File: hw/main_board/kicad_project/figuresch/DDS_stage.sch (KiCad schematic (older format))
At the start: 12 parts

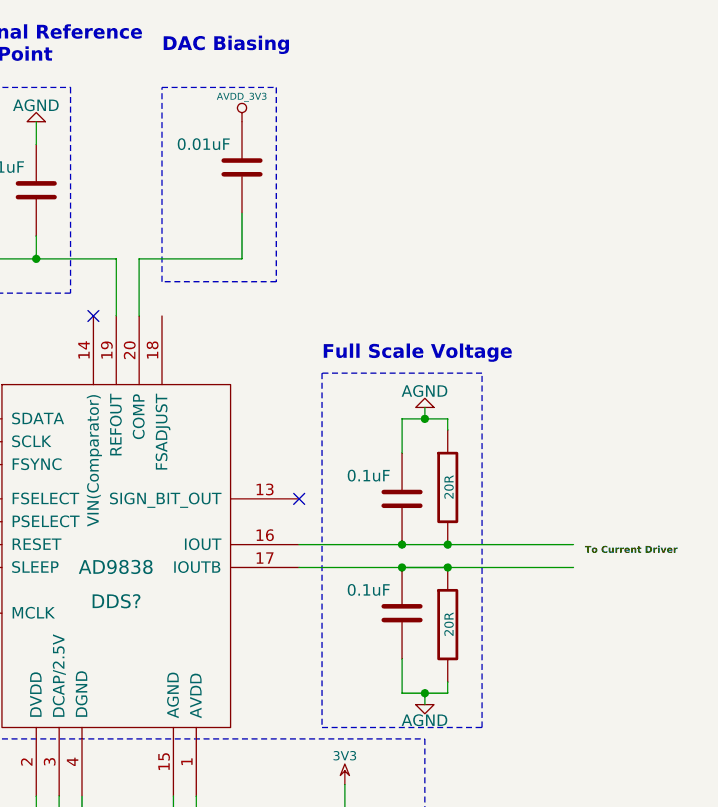
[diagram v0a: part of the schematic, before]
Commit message: started mainboard pcb layout, fixing small things in schematic, TODO: schematic connector symbols and pads
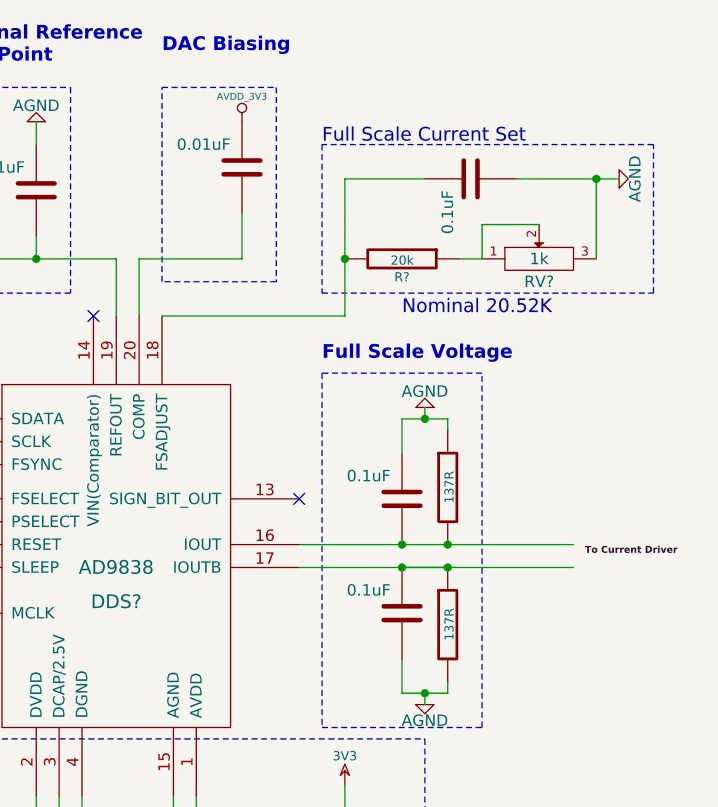
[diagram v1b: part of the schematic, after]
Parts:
- added C?: 0.1uF, symbol C
- added R?: 20k, symbol R
- added RV?: 1k, symbol POT
- R? (x2): value 20R -> 137R
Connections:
- wire segments 38 -> 46
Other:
- note added: "Full Scale Current Set"
- note added: "Nominal 20.52K\n"
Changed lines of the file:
@@
 LIBS:contrib
 LIBS:valves
-LIBS:tDCS_driver-cache
+LIBS:DDS_stage-cache
 EELAYER 24 0
 EELAYER END
@@
 P 6800 3250
 F 0 "R?" H 6880 3250 40  0001 C CNN
-F 1 "20R" V 6807 3251 40  0000 C CNN
+F 1 "137R" V 6807 3251 40  0000 C CNN
 F 2 "" V 6730 3250 30  0000 C CNN
 F 3 "" H 6800 3250 30  0000 C CNN
@@
 P 6800 3850
 F 0 "R?" V 6880 3850 40  0001 C CNN
-F 1 "20R" V 6807 3851 40  0000 C CNN
+F 1 "137R" V 6807 3851 40  0000 C CNN
 F 2 "" V 6730 3850 30  0000 C CNN
 F 3 "" H 6800 3850 30  0000 C CNN
@@
 Text Label 7400 3550 0    30   ~ 6
 To Current Driver
+$Comp
+L R R?
+U 1 1 5317FBD1
+P 6600 2250
+F 0 "R?" V 6680 2250 40  0000 C CNN
+F 1 "20k" V 6607 2251 40  0000 C CNN
+F 2 "" V 6530 2250 30  0000 C CNN
+F 3 "" H 6600 2250 30  0000 C CNN
+	1    6600 2250
+	0    1    1    0
+$EndComp
+$Comp
+L POT RV?
+U 1 1 5317FBFE
+P 7200 2250
+F 0 "RV?" H 7200 2150 50  0000 C CNN
+F 1 "1k" H 7200 2250 50  0000 C CNN
+F 2 "" H 7200 2250 60  0000 C CNN
+F 3 "" H 7200 2250 60  0000 C CNN
+	1    7200 2250
+	1    0    0    -1
+$EndComp
+$Comp
+L C C?
+U 1 1 5317FC10
+P 6900 1900
+F 0 "C?" H 6950 2000 50  0001 L CNN
+F 1 "0.1uF" H 6950 1800 50  0000 L CNN
+F 2 "" H 6900 1900 60  0001 C CNN
+F 3 "" H 6900 1900 60  0001 C CNN
+	1    6900 1900
+	0    1    1    0
+$EndComp
+Wire Wire Line
+	6950 2250 6950 2100
+Wire Wire Line
+	6950 2100 7200 2100
+Wire Wire Line
+	6950 2250 6850 2250
+Wire Wire Line
+	7100 1900 7550 1900
+Wire Wire Line
+	7450 1900 7450 2250
+Wire Wire Line
+	6700 1900 6350 1900
+Wire Wire Line
+	6350 1900 6350 2500
+Wire Wire Line
+	6350 2500 5550 2500
+Connection ~ 6350 2250
+$Comp
+L AGND #PWR?
+U 1 1 5317FD85
+P 7550 1900
+F 0 "#PWR?" H 7550 1900 40  0001 C CNN
+F 1 "AGND" H 7550 1830 50  0000 C CNN
+F 2 "" H 7550 1900 60  0001 C CNN
+F 3 "" H 7550 1900 60  0001 C CNN
+	1    7550 1900
+	0    -1   -1   0
+$EndComp
+Connection ~ 7450 1900
+Wire Notes Line
+	6250 1750 6250 2400
+Wire Notes Line
+	6250 2400 7700 2400
+Wire Notes Line
+	7700 2400 7700 1750
+Wire Notes Line
+	7700 1750 6250 1750
+Text Notes 6250 1750 0    60   ~ 0
+Full Scale Current Set
+Text Notes 6600 2500 0    60   ~ 0
+Nominal 20.52K\n
 $EndSCHEMATC

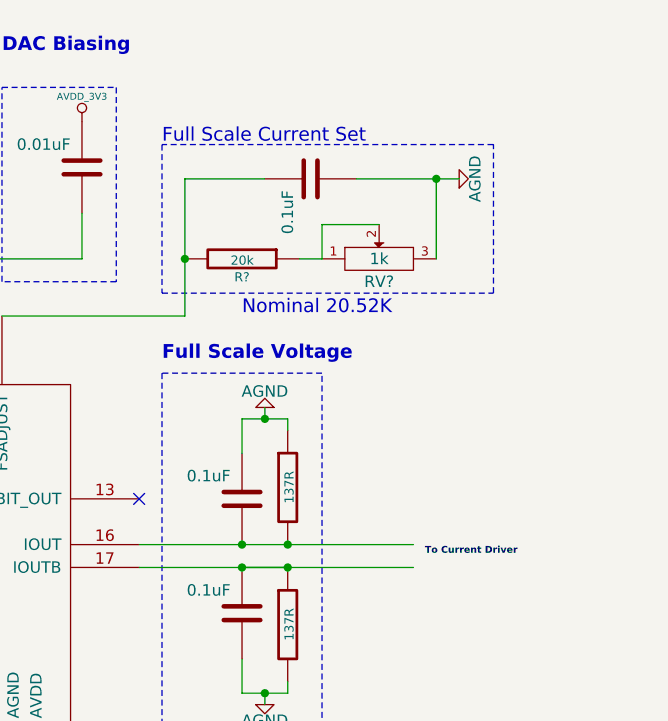
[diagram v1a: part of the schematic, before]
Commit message: Converting keepnote notes to thorough design documentation, starting with BRD1
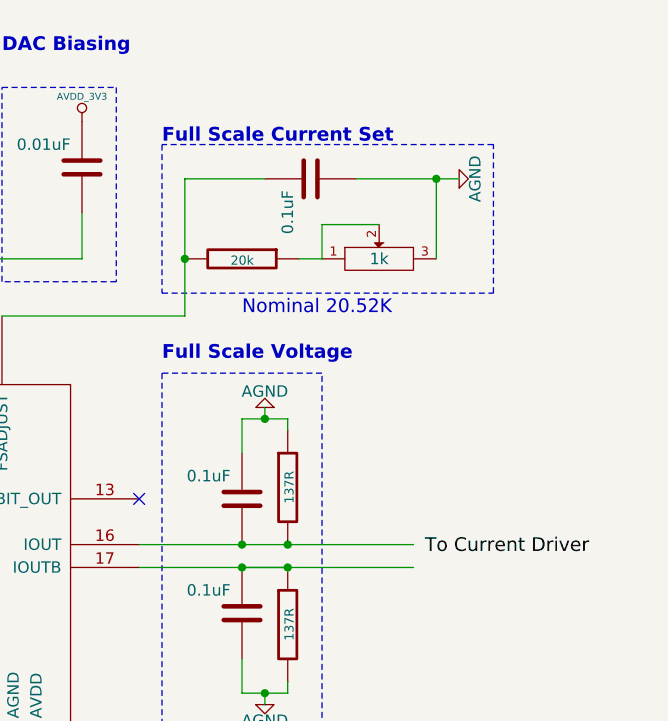
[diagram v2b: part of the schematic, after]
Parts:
- gave numbers to parts that had none: 4
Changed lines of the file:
@@
 LIBS:contrib
 LIBS:valves
-LIBS:DDS_stage-cache
+LIBS:tDCS_driver-cache
 EELAYER 24 0
 EELAYER END
@@
 NoConn ~ 6150 3300
 $Comp
-L R R?
+L R R2
 U 1 1 53123DF8
 P 6800 3250
-F 0 "R?" H 6880 3250 40  0001 C CNN
+F 0 "R2" H 6880 3250 40  0001 C CNN
 F 1 "137R" V 6807 3251 40  0000 C CNN
 F 2 "" V 6730 3250 30  0000 C CNN
@@
 $EndComp
 $Comp
-L R R?
+L R R3
 U 1 1 53123E05
 P 6800 3850
-F 0 "R?" V 6880 3850 40  0001 C CNN
+F 0 "R3" V 6880 3850 40  0001 C CNN
 F 1 "137R" V 6807 3851 40  0000 C CNN
 F 2 "" V 6730 3850 30  0000 C CNN
@@
 Text Notes 6250 2700 0    60   ~ 12
 Full Scale Voltage
-Text Label 7400 3550 0    30   ~ 6
+Text Label 7400 3550 0    60   ~ 0
 To Current Driver
 $Comp
-L R R?
+L R R1
 U 1 1 5317FBD1
 P 6600 2250
-F 0 "R?" V 6680 2250 40  0000 C CNN
+F 0 "R1" V 6680 2250 40  0001 C CNN
 F 1 "20k" V 6607 2251 40  0000 C CNN
 F 2 "" V 6530 2250 30  0000 C CNN
@@
 $EndComp
 $Comp
-L POT RV?
+L POT RV1
 U 1 1 5317FBFE
 P 7200 2250
-F 0 "RV?" H 7200 2150 50  0000 C CNN
+F 0 "RV1" H 7200 2150 50  0001 C CNN
 F 1 "1k" H 7200 2250 50  0000 C CNN
 F 2 "" H 7200 2250 60  0000 C CNN
@@
 Wire Notes Line
 	7700 1750 6250 1750
-Text Notes 6250 1750 0    60   ~ 0
+Text Notes 6250 1750 0    60   ~ 12
 Full Scale Current Set
 Text Notes 6600 2500 0    60   ~ 0
